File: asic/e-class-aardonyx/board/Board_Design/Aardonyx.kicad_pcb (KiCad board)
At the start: 4 copper layers, 298 parts, among them J1 USB_B_6PIN, J10 Conn_1x6_F, J11 Conn_1x6_F, J12 Conn_1x3_M, J13 Conn_1x8_F, J14 Conn_1x6_F, J15 Conn_1x10, J16 Conn_1x8_F, J17 USB_OTG, J18 Conn_1x3_M, J19 Conn_1x3_M, J2 Conn_1x8, J3 Conn_1x3_M, J4 Conn_1x4, J5 PJ-202H PWRJACK, J6 Conn_1x3_M, J7 Conn_1x4, J8 Conn_1x3_M, J9 Conn_1x8, Q1 FDN339AN, SW1 SW_SPST, SW2 FSM2JSMAATR, SW3 SW_DIP_x03, U1 FT2232H, U10 TPS7A7002DDAR, U11 ADM1085, U12 ADM1085, U13 TPS7A7002DDAR, U14 74AUP1G09GW, U15 SKT32E, U16 93LC56BT-I_OT, U2 IS42S32160F-TSOP2, U3 CDCE913PW, U4 TPS54627DDAR, U5 CAT24M01WI-GT3, U6 IS25LP256x-xM, U7 ADC108S102CIMTX, U8 LSF0108PWR, U9 LSF0108PWR, Y1 12MHz, Y2 27MHz

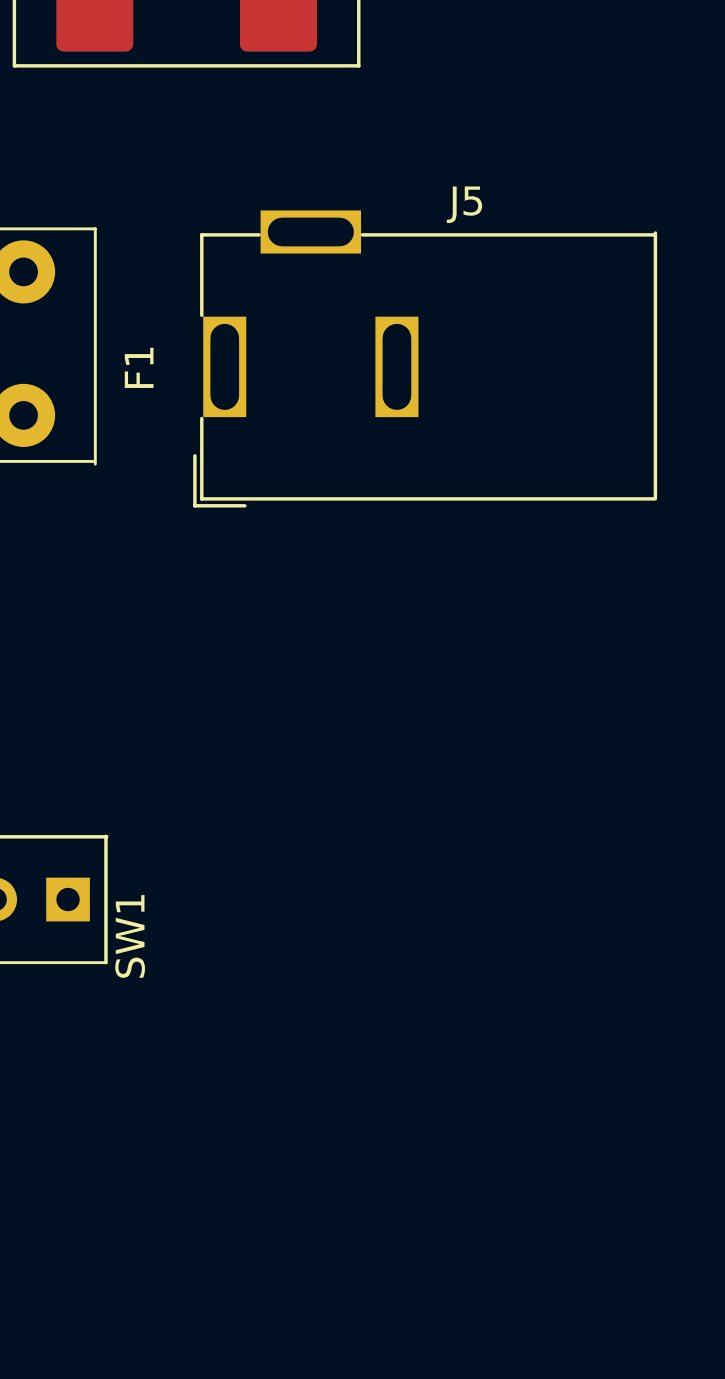
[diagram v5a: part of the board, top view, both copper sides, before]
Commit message: add skt sock footprint & componont update
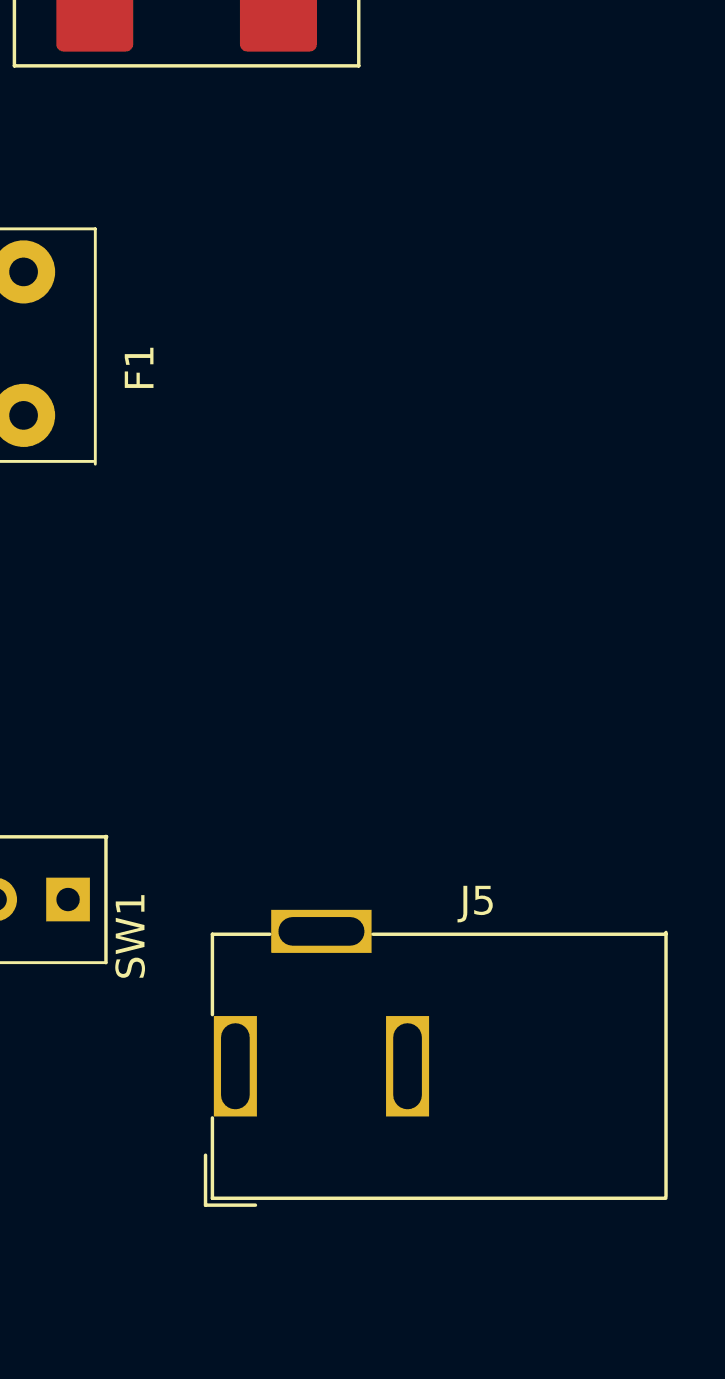
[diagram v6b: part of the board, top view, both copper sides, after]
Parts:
- moved J5 24.4 mm to (252.4, 149.2)
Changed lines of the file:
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@@
   )
   (module Aardonyx:Pwr_Jack_DC_PJ-202AH_Horizontal (layer F.Cu)
-    (at 252.01 124.82 90)
+    (at 252.38 149.19 90)
     (descr "Thin-pin DC Barrel Jack, https://cdn-shop.adafruit.com/datasheets/21mmdcjackDatasheet.pdf")
     (tags "Power Jack")

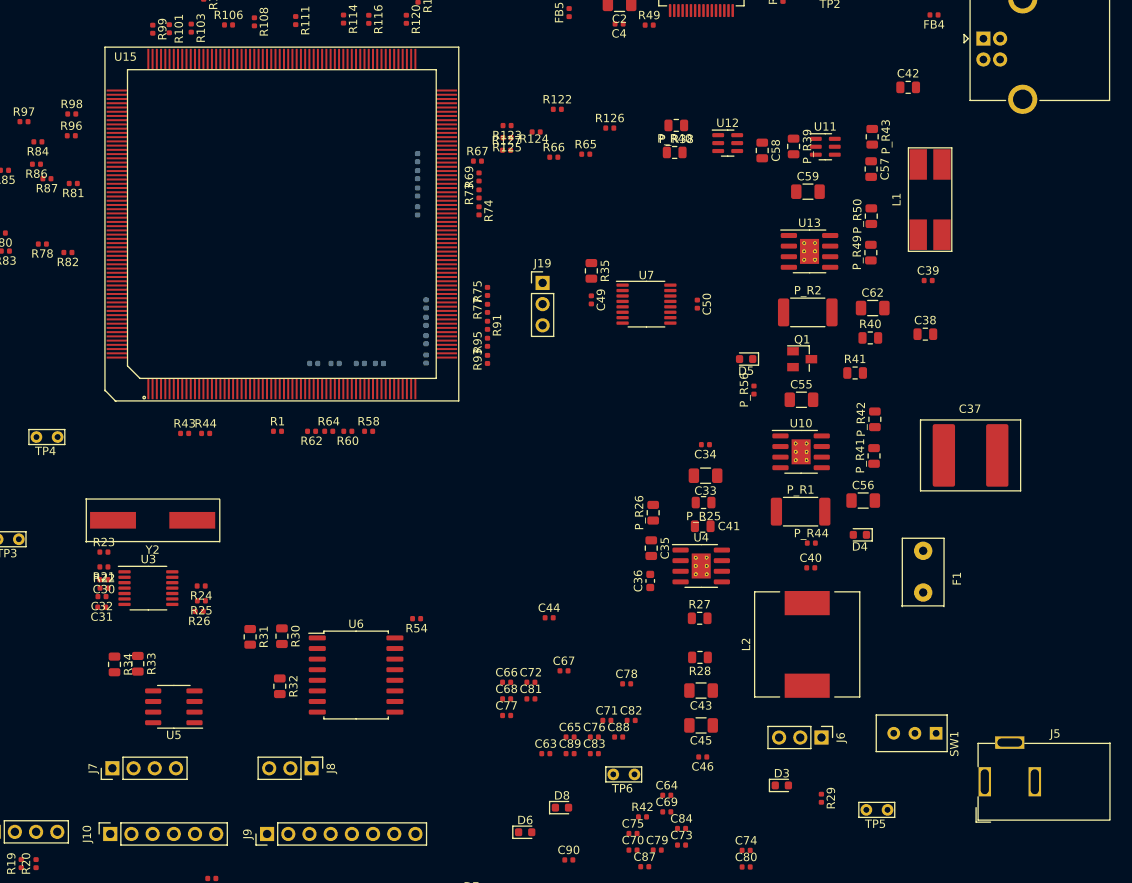
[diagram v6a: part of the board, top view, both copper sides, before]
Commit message: update component placement
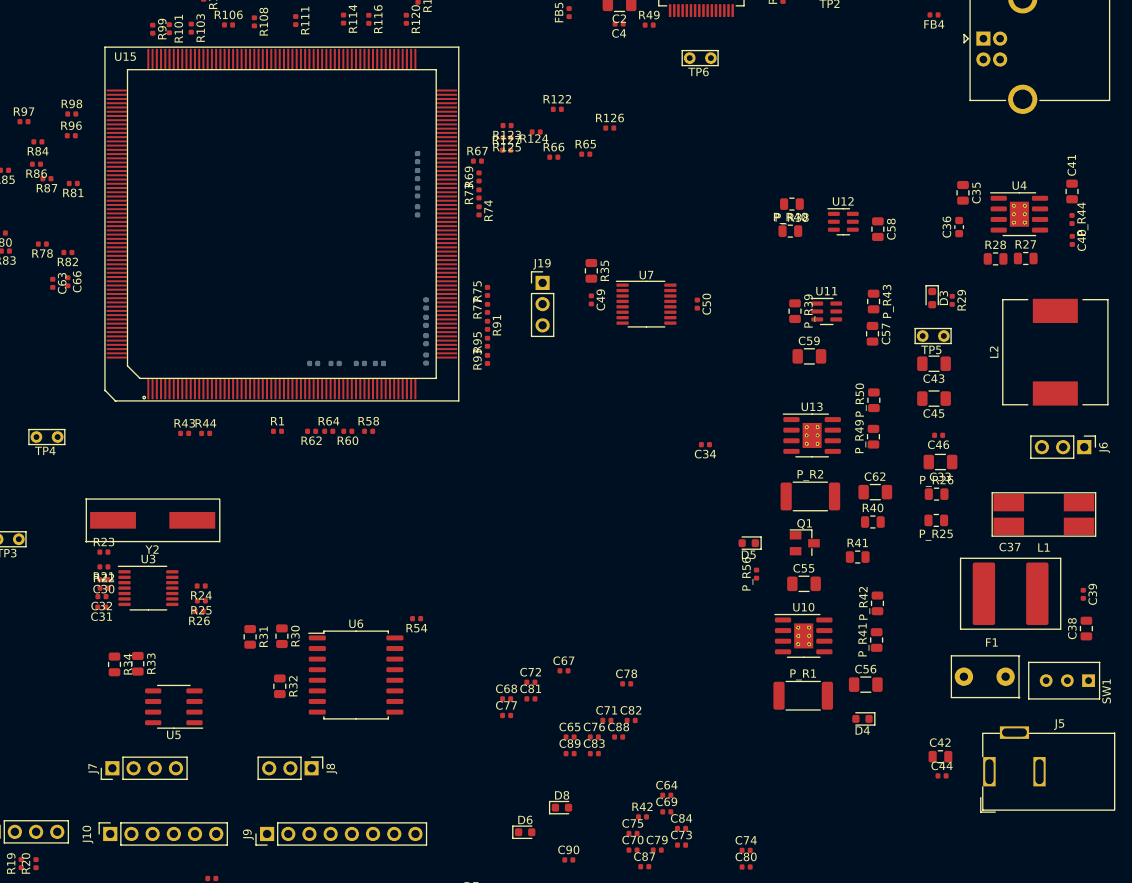
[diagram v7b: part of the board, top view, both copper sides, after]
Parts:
- moved TP6 86.3 mm to (217.0, 62.5)
- moved C63 81.7 mm to (140.7, 89.5), turned to 270 degrees
- moved C42 80.3 mm to (247.1, 146.2)
- moved C66 71.2 mm to (142.5, 89.3), turned to 270 degrees
- moved R29 61.7 mm to (248.5, 91.5)
- moved D3 61.1 mm to (246.1, 91.2), turned to 270 degrees
- moved C41 59.7 mm to (262.8, 78.4), turned to 270 degrees
- moved R28 59.5 mm to (253.7, 86.5), turned to 0 degrees
- moved R27 58.2 mm to (257.3, 86.5)
- moved TP5 57.2 mm to (244.9, 95.8)
- moved U4 56.8 mm to (256.5, 81.2)
- moved C35 56.6 mm to (249.8, 78.6)
- moved C36 56.3 mm to (249.3, 82.7)
- moved C44 50.8 mm to (247.3, 148.5)
- moved C40 50.2 mm to (262.9, 84.3), turned to 270 degrees
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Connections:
- C11 pad 1: VCC -> ~
- C12 pad 1: VCC -> ~
- C13 pad 1: VCC -> ~
- C14 pad 1: VCC -> V3P3
- C15 pad 1: VCC -> V3P3
- C16 pad 1: VCC -> V3P3
- C17 pad 1: VCC -> V3P3
- C18 pad 1: VCC -> V3P3
- C19 pad 1: VCC -> V3P3
- C2 pad 1: VCC -> ~
- C20 pad 1: VCC -> V3P3
- C21 pad 1: VCC -> V3P3
- C22 pad 1: VCC -> V3P3
- C23 pad 1: VCC -> V3P3
- C24 pad 1: VCC -> V3P3
- C25 pad 1: VCC -> V3P3
- C26 pad 1: VCC -> V3P3
- C27 pad 1: VCC -> V3P3
- C28 pad 1: VCC -> V3P3
- C29 pad 1: VCC -> V3P3
- C30 pad 1: VCC -> ~
- C31 pad 1: VCC -> V3P3
- C32 pad 1: VCC -> V3P3
- C33 pad 1: VCC -> ~
- C34 pad 1: VCC -> ~
- C4 pad 1: VCC -> ~
- C41 pad 1: VCC -> ~
- C42 pad 1: VCC -> ~
- C43 pad 1: VCC -> ~
- C44 pad 1: VCC -> ~
- C45 pad 1: VCC -> ~
- C46 pad 1: VCC -> ~
- C47 pad 1: VCC -> V3P3
- C48 pad 1: VCC -> V3P3
- C49 pad 1: VCC -> ~
- C50 pad 1: VCC -> V3P3
- C51 pad 1: VCC -> V3P3
- C52 pad 1: VCC -> ~
- C53 pad 1: VCC -> V3P3
- C54 pad 1: VCC -> ~
- C55 pad 1: VCC -> V5P0
- C56 pad 1: VCC -> V3P3
- C59 pad 1: VCC -> V5P0
- C61 pad 1: VCC -> V3P3
- C62 pad 1: VCC -> V1P8
- C63 pad 1: VCC -> V1P8
- C64 pad 1: VCC -> V1P8
- C65 pad 1: VCC -> V3P3
- C66 pad 1: VCC -> V1P8
- C67 pad 1: VCC -> V1P8
- C68 pad 1: VCC -> V3P3
- C69 pad 1: VCC -> V1P8
- C7 pad 1: VCC -> V3P3
- C70 pad 1: VCC -> V1P8
- C71 pad 1: VCC -> V3P3
- C72 pad 1: VCC -> V1P8
- C73 pad 1: VCC -> V1P8
- C74 pad 1: VCC -> V3P3
- C75 pad 1: VCC -> V1P8
- C76 pad 1: VCC -> V1P8
- C77 pad 1: VCC -> V3P3
- C78 pad 1: VCC -> V1P8
- C79 pad 1: VCC -> V1P8
- C80 pad 1: VCC -> V3P3
- C81 pad 1: VCC -> V1P8
- C82 pad 1: VCC -> V1P8
- C83 pad 1: VCC -> V3P3
- C84 pad 1: VCC -> V1P8
- C86 pad 1: VCC -> V3P3
- C87 pad 1: VCC -> V1P8
- C88 pad 1: VCC -> V3P3
- C89 pad 1: VCC -> V1P8
- C90 pad 1: VCC -> V3P3
- C92 pad 1: VCC -> V3P3
- FB1 pad 2: VCC -> ~
- FB2 pad 2: VCC -> V3P3
- FB3 pad 2: VCC -> V3P3
- FB4 pad 2: VCC -> ~
- J10 pad 6: VCC -> V3P3
- J11 pad 5: VCC -> V3P3
- J12 pad 1: VCC -> V3P3
- J12 pad 2: VCC -> ~
- J12 pad 3: VCC -> V5P0
- J13 pad 2: VCC -> ~
- J13 pad 4: VCC -> V3P3
- J13 pad 5: VCC -> V5P0
- J15 pad 3: VCC -> V3P3
- J18 pad 1: VCC -> ~
- J18 pad 2: VCC -> ~
- J18 pad 3: VCC -> ~
- J19 pad 1: VCC -> V5P0
- J19 pad 2: VCC -> ~
- J19 pad 3: VCC -> V3P3
- J2 pad 1: VCC -> V3P3
- J4 pad 1: VCC -> V3P3
- J6 pad 1: VCC -> ~
- J6 pad 2: VCC -> V5P0
- J6 pad 3: VCC -> ~
- J7 pad 1: VCC -> V3P3
- J9 pad 1: VCC -> V3P3
- L1 pad 4: VCC -> ~
- L2 pad 2: VCC -> ~
- P_R1 pad 1: VCC -> V3P3
- P_R2 pad 1: VCC -> V1P8
- P_R25 pad 1: VCC -> ~
- P_R38 pad 1: VCC -> V1P8
- P_R39 pad 1: VCC -> V3P3
- P_R43 pad 1: VCC -> V3P3
- P_R44 pad 1: VCC -> V3P3
- P_R56 pad 1: VCC -> V1P8
- R1 pad 1: VCC -> V3P3
- R11 pad 1: VCC -> V3P3
- R13 pad 1: VCC -> V3P3
- R131 pad 1: VCC -> V3P3
- R132 pad 1: VCC -> V1P8
- R15 pad 1: VCC -> V3P3
- R17 pad 1: VCC -> V3P3
- R19 pad 1: VCC -> V3P3
- R20 pad 1: VCC -> V3P3
- R21 pad 1: VCC -> V3P3
- R22 pad 1: VCC -> ~
- R28 pad 1: VCC -> ~
- R29 pad 1: VCC -> V5P0
- R30 pad 1: VCC -> V3P3
- R31 pad 1: VCC -> V3P3
- R32 pad 1: VCC -> V3P3
- R33 pad 1: VCC -> V3P3
- R34 pad 1: VCC -> V3P3
- R35 pad 2: VCC -> V3P3
- R36 pad 1: VCC -> ~
- R37 pad 1: VCC -> ~
- R40 pad 1: VCC -> V1P8
- R41 pad 2: VCC -> V1P8
- R45 pad 1: VCC -> V3P3
- R48 pad 1: VCC -> V3P3
- R5 pad 1: VCC -> V3P3
- R50 pad 1: VCC -> ~
- R51 pad 1: VCC -> V3P3
- R55 pad 1: VCC -> V3P3
- R7 pad 1: VCC -> V3P3
- R9 pad 1: VCC -> V3P3
- TP5 pad 1: VCC -> ~
- U1 pad 12: VCC -> ~
- U1 pad 20: VCC -> V3P3
- U1 pad 31: VCC -> V3P3
- U1 pad 37: VCC -> ~
- U1 pad 42: VCC -> V3P3
- U1 pad 49: VCC -> ~
- U1 pad 50: VCC -> V3P3
- U1 pad 56: VCC -> V3P3
- U1 pad 64: VCC -> ~
- U10 pad 2: VCC -> V5P0
- U10 pad 3: VCC -> V5P0
- U11 pad 1: VCC -> ~
- U11 pad 6: VCC -> V3P3
- U12 pad 1: VCC -> ~
- U12 pad 6: VCC -> V3P3
- U13 pad 3: VCC -> V5P0
- U14 pad 5: VCC -> V3P3
- U15 pad 109: VCC -> V1P8
- U15 pad 137: VCC -> V1P8
- U15 pad 143: VCC -> V3P3
- U15 pad 147: VCC -> V1P8
- U15 pad 15: VCC -> V3P3
- U15 pad 158: VCC -> V1P8
- U15 pad 160: VCC -> V3P3
- U15 pad 165: VCC -> V1P8
- U15 pad 173: VCC -> V1P8
- U15 pad 175: VCC -> V3P3
- U15 pad 177: VCC -> V1P8
- U15 pad 189: VCC -> V1P8
- U15 pad 207: VCC -> V3P3
- U15 pad 210: VCC -> V1P8
- U15 pad 211: VCC -> V1P8
- U15 pad 219: VCC -> V1P8
- U15 pad 222: VCC -> V1P8
- U15 pad 224: VCC -> V3P3
- U15 pad 234: VCC -> V1P8
- U15 pad 237: VCC -> V1P8
- U15 pad 30: VCC -> V1P8
- U15 pad 32: VCC -> V3P3
- U15 pad 45: VCC -> V1P8
- U15 pad 47: VCC -> V3P3
- U15 pad 79: VCC -> V3P3
- U15 pad 94: VCC -> V1P8
- U15 pad 96: VCC -> V3P3
- U16 pad 6: VCC -> V3P3
- U2 pad 1: VCC -> V3P3
- U2 pad 15: VCC -> V3P3
- U2 pad 29: VCC -> V3P3
- U2 pad 3: VCC -> V3P3
- U2 pad 35: VCC -> V3P3
- U2 pad 41: VCC -> V3P3
- U2 pad 43: VCC -> V3P3
- U2 pad 49: VCC -> V3P3
- U2 pad 55: VCC -> V3P3
- U2 pad 75: VCC -> V3P3
- U2 pad 81: VCC -> V3P3
- U2 pad 9: VCC -> V3P3
- U3 pad 3: VCC -> ~
- U3 pad 6: VCC -> V3P3
- U3 pad 7: VCC -> V3P3
- U4 pad 8: VCC -> ~
- U5 pad 8: VCC -> V3P3
- U6 pad 2: VCC -> V3P3
- U7 pad 13: VCC -> V3P3
- U7 pad 2: VCC -> ~
- U8 pad 2: VCC -> V3P3
- U9 pad 2: VCC -> V3P3

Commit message: update component place
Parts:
- C66, C69, C72: moved to B.Cu
- R57, R59, R61, R63, R68, R70, R71, R72, R76, R90, R92, R94: moved to F.Cu
- moved C87 105.6 mm to (155.4, 70.0), turned to 270 degrees
- moved C64 104.7 mm to (147.5, 70.1), turned to 270 degrees
- moved C84 102.1 mm to (158.9, 70.2), turned to 270 degrees
- moved C75 93.2 mm to (173.2, 69.9), turned to 270 degrees
- moved C89 90.7 mm to (153.0, 69.9), turned to 270 degrees
- moved C78 78.8 mm to (168.6, 70.1), turned to 270 degrees
- moved C26 78.6 mm to (172.9, 47.3), turned to 180 degrees
- moved C22 78.6 mm to (172.9, 30.0), turned to 0 degrees
- moved C81 77.3 mm to (163.2, 70.2), turned to 270 degrees
- moved C69 75.6 mm to (177.8, 86.6), turned to 90 degrees
- moved C29 74.4 mm to (169.8, 47.5), turned to 270 degrees
- moved C23 71.0 mm to (167.5, 30.5), turned to 180 degrees
- moved C21 70.9 mm to (167.2, 47.5), turned to 0 degrees
- moved R46 68.9 mm to (133.6, 39.8)
- moved SW2 68.9 mm to (143.1, 39.4)
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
